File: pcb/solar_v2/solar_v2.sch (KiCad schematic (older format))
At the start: 30 parts, among them P3 TX/RX, P5 ISP, P6 ANT, Y1 8MHZ

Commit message: updated schema
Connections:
- net SCA is gone; now on net SDA: P?.4 (P4)
- net SCL: now also IC?.28 ((PCINT13/SCL/ADC5)PC5)
- net SDA: now reaches IC?.27 ((PCINT12/SDA/ADC4)PC4)
- net RX: no longer names the net of IC?.2 ((PCINT16/RXD)PD0), P3.1 (P1)
- net TX: no longer names the net of IC?.3 ((PCINT17/TXD)PD1), P3.2 (P2)
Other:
- moved on the sheet: P3, R?
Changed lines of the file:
@@
 L CONN_01X02 P3
 U 1 1 5A883E85
-P 800 4500
-F 0 "P3" H 800 4650 50  0000 C CNN
-F 1 "TX/RX" V 900 4500 50  0000 C CNN
-F 2 "Pin_Headers:Pin_Header_Straight_1x02" H 800 4500 50  0001 C CNN
-F 3 "" H 800 4500 50  0000 C CNN
-	1    800  4500
-	-1   0    0    1
-$EndComp
-Text GLabel 1300 4450 2    60   Input ~ 0
-TX
-Text GLabel 1100 4550 2    60   Input ~ 0
-RX
-Wire Wire Line
-	1300 4450 1000 4450
-Wire Wire Line
-	1100 4550 1000 4550
+P 4550 2900
+F 0 "P3" H 4550 3050 50  0000 C CNN
+F 1 "TX/RX" V 4650 2900 50  0000 C CNN
+F 2 "Pin_Headers:Pin_Header_Straight_1x02" H 4550 2900 50  0001 C CNN
+F 3 "" H 4550 2900 50  0000 C CNN
+	1    4550 2900
+	1    0    0    -1
+$EndComp
 $Comp
 L RFM69 RF1
@@
 	9350 1550 9350 1600
 Text GLabel 9450 1700 2    60   Input ~ 0
-SCA
+SDA
 Wire Wire Line
 	9450 1550 9450 1700
 Wire Wire Line
 	8800 2300 8800 2400
-Text GLabel 3700 2700 1    60   Input ~ 0
+Text GLabel 4700 2650 1    60   Input ~ 0
 RST
 $Comp
 L R R?
 U 1 1 5AE8C74E
-P 3950 2700
-F 0 "R?" V 4030 2700 50  0000 C CNN
-F 1 "10k" V 3950 2700 50  0000 C CNN
-F 2 "Resistors_SMD:R_0805_HandSoldering" V 3880 2700 50  0001 C CNN
-F 3 "" H 3950 2700 50  0000 C CNN
-	1    3950 2700
-	0    1    1    0
-$EndComp
-Text GLabel 4400 2700 2    60   Input ~ 0
+P 5000 2700
+F 0 "R?" V 5080 2700 50  0000 C CNN
+F 1 "10k" V 5000 2700 50  0000 C CNN
+F 2 "Resistors_SMD:R_0805_HandSoldering" V 4930 2700 50  0001 C CNN
+F 3 "" H 5000 2700 50  0000 C CNN
+	1    5000 2700
+	0    1    1    0
+$EndComp
+Text GLabel 5350 2700 2    60   Input ~ 0
 3.3V
-Wire Wire Line
-	3300 2700 3800 2700
-Text GLabel 3500 2850 2    60   Input ~ 0
-RX
-Text GLabel 3700 2950 2    60   Input ~ 0
-TX
-Wire Wire Line
-	3500 2850 3300 2850
-Wire Wire Line
-	3700 2950 3300 2950
 Text GLabel 3700 3250 2    60   Input ~ 0
 V_MESS_ENABLE
@@
 Wire Wire Line
 	3750 1750 3300 1750
-Wire Wire Line
-	4400 2700 4100 2700
 $Comp
 L BC556 Q?
@@
 Wire Wire Line
 	6050 6300 6050 6400
+Wire Wire Line
+	5350 2700 5150 2700
+Wire Wire Line
+	4850 2700 3300 2700
+Wire Wire Line
+	4700 2650 4700 2700
+Connection ~ 4700 2700
+Wire Wire Line
+	4350 2850 3300 2850
+Wire Wire Line
+	3300 2950 4350 2950
+Text GLabel 3500 2600 2    60   Input ~ 0
+SCL
+Text GLabel 3800 2500 2    60   Input ~ 0
+SDA
+Wire Wire Line
+	3800 2500 3300 2500
+Wire Wire Line
+	3500 2600 3300 2600
 $EndSCHEMATC

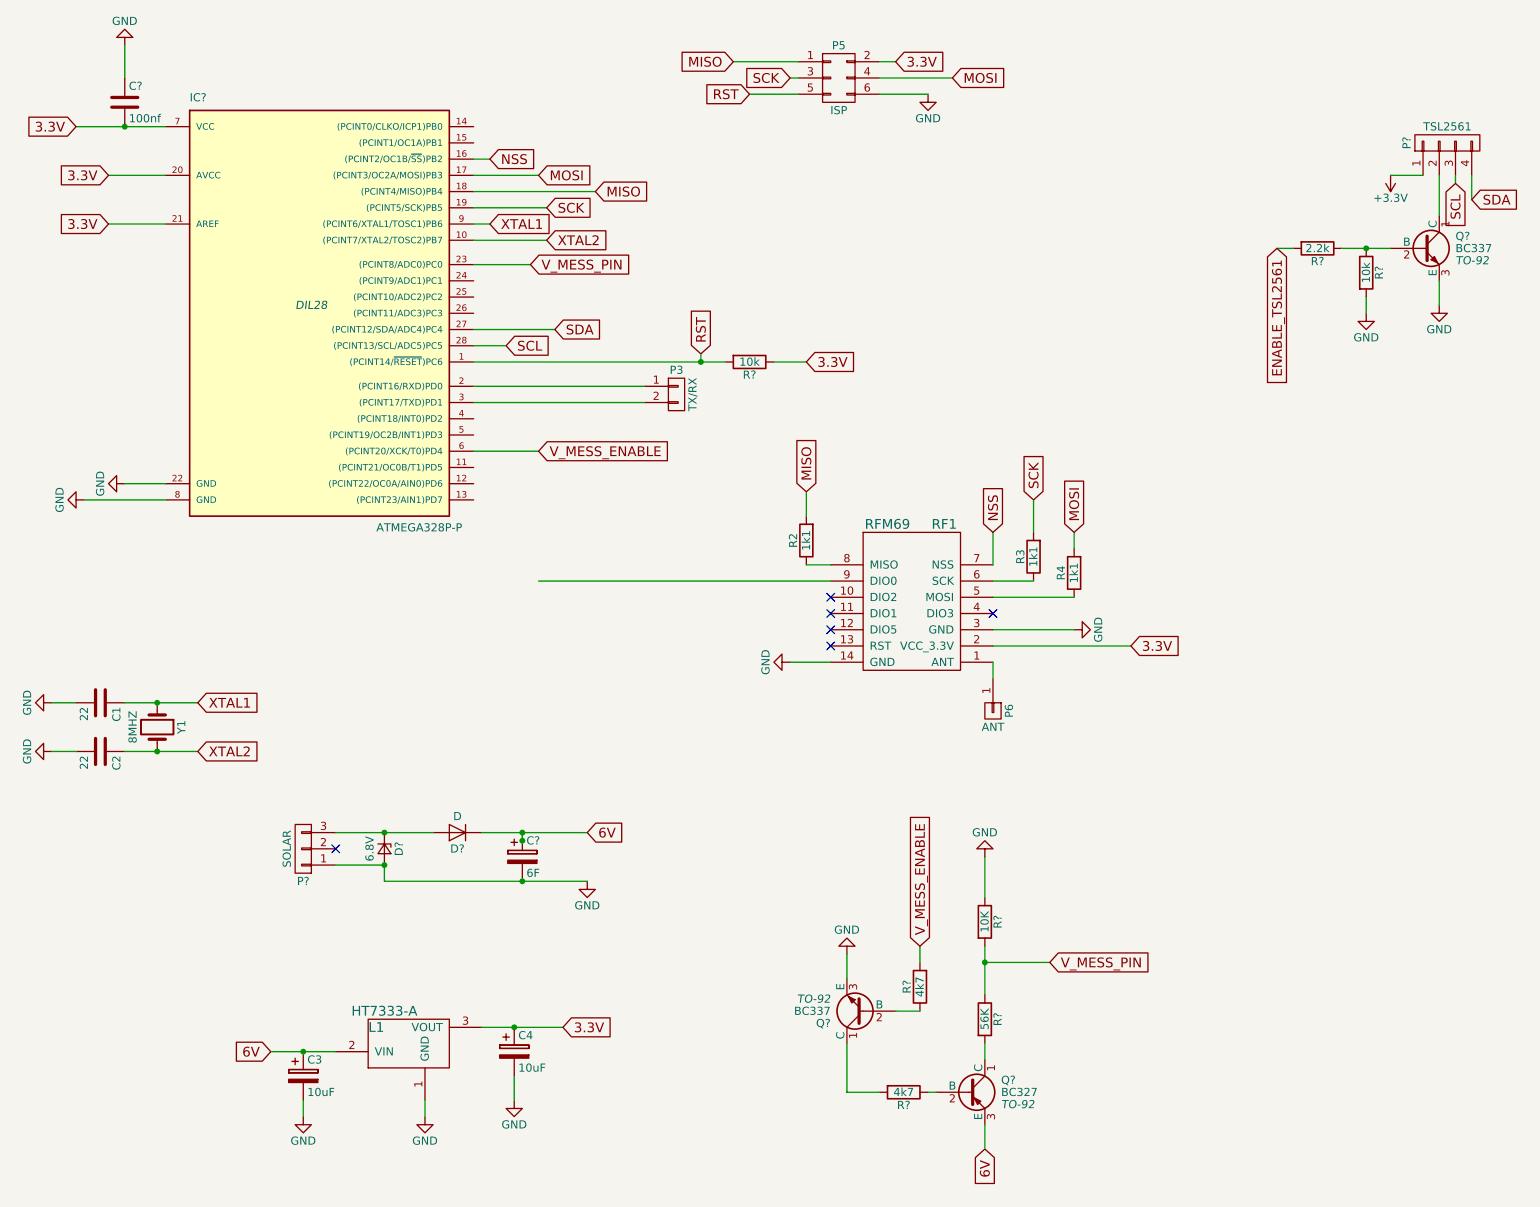
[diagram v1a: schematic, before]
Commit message: added NTC 10k
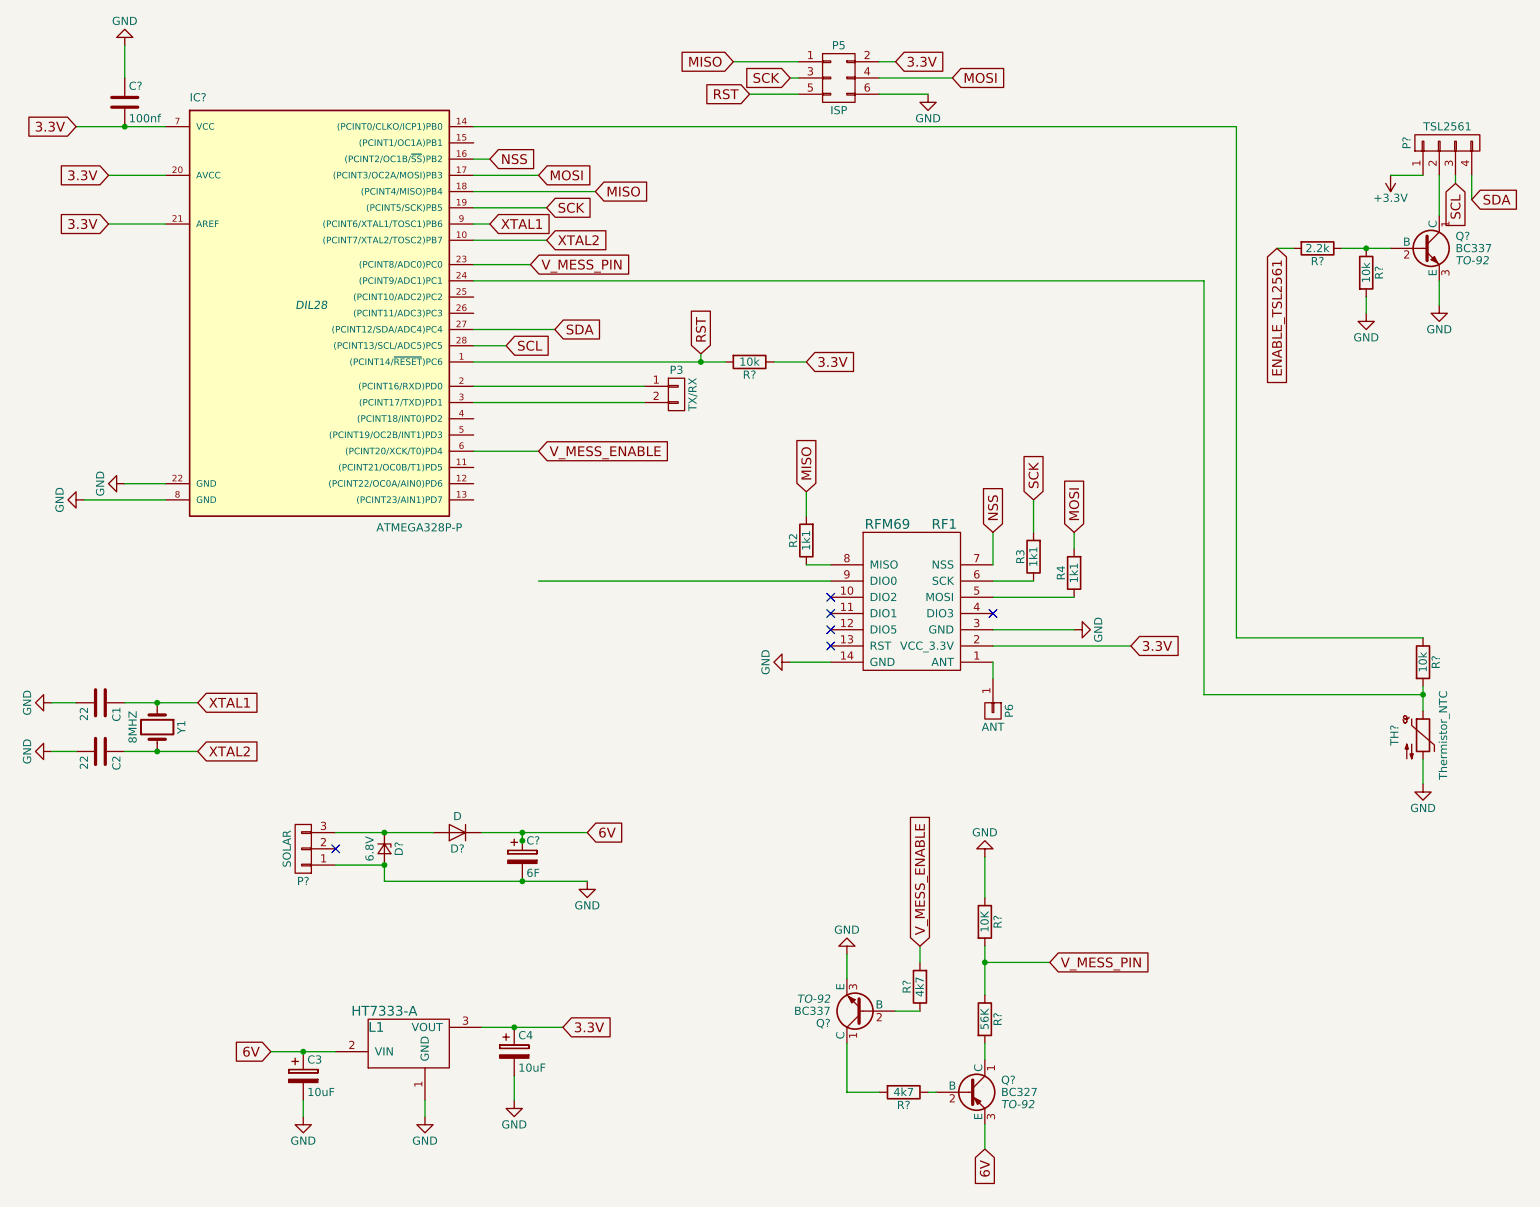
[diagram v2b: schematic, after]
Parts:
- added R?: 10k, symbol R
- added TH?: Thermistor_NTC, symbol Thermistor_NTC
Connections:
- net GND: now also TH?.2
- net at IC?.14 ((PCINT0/CLKO/ICP1)PB0): now also R?.1
- net at IC?.24 ((PCINT9/ADC1)PC1): now also R?.2, TH?.1
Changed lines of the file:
@@
 Wire Wire Line
 	3500 2600 3300 2600
+$Comp
+L R R?
+U 1 1 5AEF5A46
+P 9150 4550
+F 0 "R?" V 9230 4550 50  0000 C CNN
+F 1 "10k" V 9150 4550 50  0000 C CNN
+F 2 "" V 9080 4550 50  0000 C CNN
+F 3 "" H 9150 4550 50  0000 C CNN
+	1    9150 4550
+	1    0    0    -1
+$EndComp
+$Comp
+L GND #PWR?
+U 1 1 5AEF6561
+P 9150 5300
+F 0 "#PWR?" H 9150 5050 50  0001 C CNN
+F 1 "GND" H 9150 5150 50  0000 C CNN
+F 2 "" H 9150 5300 50  0000 C CNN
+F 3 "" H 9150 5300 50  0000 C CNN
+	1    9150 5300
+	1    0    0    -1
+$EndComp
+$Comp
+L Thermistor_NTC TH?
+U 1 1 5AEF65F1
+P 9150 5000
+F 0 "TH?" V 8975 5000 50  0000 C CNN
+F 1 "Thermistor_NTC" V 9275 5000 50  0000 C CNN
+F 2 "" H 9150 5050 50  0001 C CNN
+F 3 "" H 9150 5050 50  0001 C CNN
+	1    9150 5000
+	1    0    0    -1
+$EndComp
+Wire Wire Line
+	9150 5150 9150 5300
+Wire Wire Line
+	9150 4850 9150 4700
+Wire Wire Line
+	3300 2200 7800 2200
+Wire Wire Line
+	7800 2200 7800 4750
+Wire Wire Line
+	7800 4750 9150 4750
+Connection ~ 9150 4750
+Wire Wire Line
+	3300 1250 8000 1250
+Wire Wire Line
+	8000 1250 8000 4400
+Wire Wire Line
+	8000 4400 9150 4400
 $EndSCHEMATC
